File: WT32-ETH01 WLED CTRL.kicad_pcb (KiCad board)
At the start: 2 copper layers, 60 x 60 mm, 21 parts, among them J1 USB_C_Receptacle_USB2.0_14P, Q1 S8050, Q2 S8050, SW1 Reset, SW2 Boot, U1 WT32-ETH01, U2 CH340C

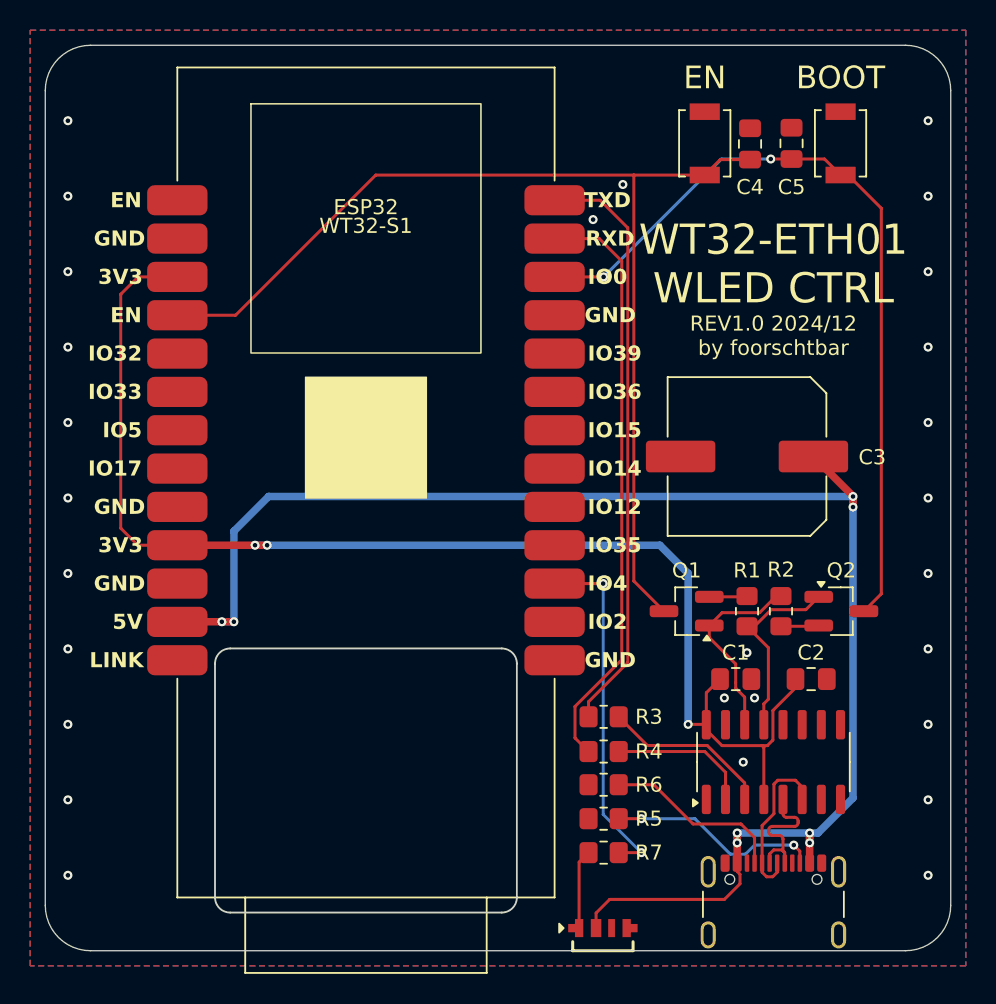
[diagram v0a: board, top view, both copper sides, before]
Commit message: Updated Board to REV2.0 - Removed usb reset circut - Added antenna cutout - Added TX/RX LEDs
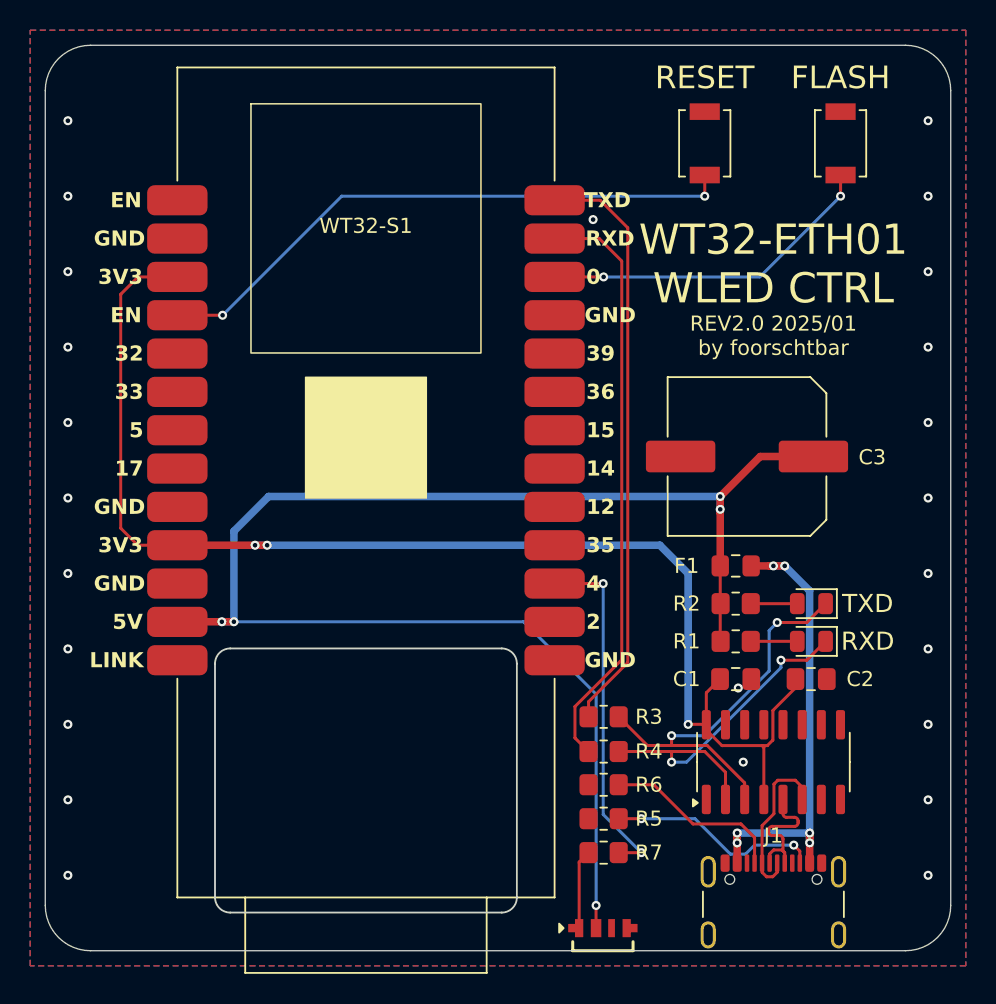
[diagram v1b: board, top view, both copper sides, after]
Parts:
- removed C4, C5: 100nF, Capacitor_SMD:C_0805_2012Metric_Pad1.18x1.45mm_HandSolder
- removed Q1, Q2: S8050, Package_TO_SOT_SMD:SOT-23_Handsoldering
- added D1: RXD, LED_SMD:LED_0805_2012Metric, F.Cu at (144.0, 95.8)
- added D2: TXD, LED_SMD:LED_0805_2012Metric, F.Cu at (144.0, 93.2)
- added F1: Fuse, Fuse:Fuse_0805_2012Metric_Pad1.15x1.40mm_HandSolder, F.Cu at (139.0, 90.8)
- R1, R2: value 10k -> 330
- moved R2 3.04 mm to (139.0, 93.2), turned to 0 degrees
- moved R1 2.14 mm to (139.0, 95.8), turned to 0 degrees
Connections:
- net Net-(U2-RXD) renamed /TXD
- net Net-(U2-TXD) renamed /RXD
- net RXD renamed MCU_RXD
- net TXD renamed MCU_TXD
- J1 pad A4: VIN -> /VBUS
- J1 pad A9: VIN -> /VBUS
- J1 pad B4: VIN -> /VBUS
- J1 pad B9: VIN -> /VBUS
- R1 pad 1: Net-(Q1-B) -> VIN
- R1 pad 2: DTR -> Net-(D1-A)
- R2 pad 1: Net-(Q2-B) -> VIN
- R2 pad 2: RTS -> Net-(D2-A)
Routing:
- net /VBUS: track 0.00 -> 33.4 mm, vias 0 -> 6
- net EN: track 72.0 -> 39.6 mm, vias 0 -> 2
- net GPIO0: track 52.9 -> 22.6 mm
- net /TXD: track 11.3 -> 27.3 mm, vias 0 -> 2
- net /RXD: track 9.44 -> 24.0 mm, vias 0 -> 2
- net RTS: track 12.8 -> 0.00 mm
- net DTR: track 12.3 -> 0.00 mm
- net Net-(D2-A): track 0.00 -> 3.08 mm
- net Net-(D1-A): track 0.00 -> 3.08 mm
- net Net-(Q2-B): track 2.45 -> 0.00 mm
- net Net-(Q1-B): track 2.45 -> 0.00 mm
- net +3.3V: track 87.6 -> 86.6 mm
- net VIN: track 103.7 -> 102.9 mm, vias 8 -> 5
- net GND: vias 28 -> 25
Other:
- board text added: "FLASH"
- board text added: "RESET"
- board text added: "REV2.0 2025/01 by foorschtbar"
- board text added: "REV2.0 2025/01 by foorschtbar github.com/foorschtbar/WT32-ETH01-WLED-CTRL"
- board text added: "RXD"
- board text added: "TXD"
- board text removed: "BOOT"
- board text removed: "EN"
- board text removed: "REV1.0 2024/12 by foorschtbar"
- board text removed: "REV1.0 2024/12 by foorschtbar github.com/foorschtbar/WT32-ETH01-WLED-CTRL"
